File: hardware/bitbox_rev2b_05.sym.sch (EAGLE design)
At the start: 65 parts, among them IC3 LM317MSTT3, Q1 8MHz, U1 USD-SOCKETNEW, X2 2510-

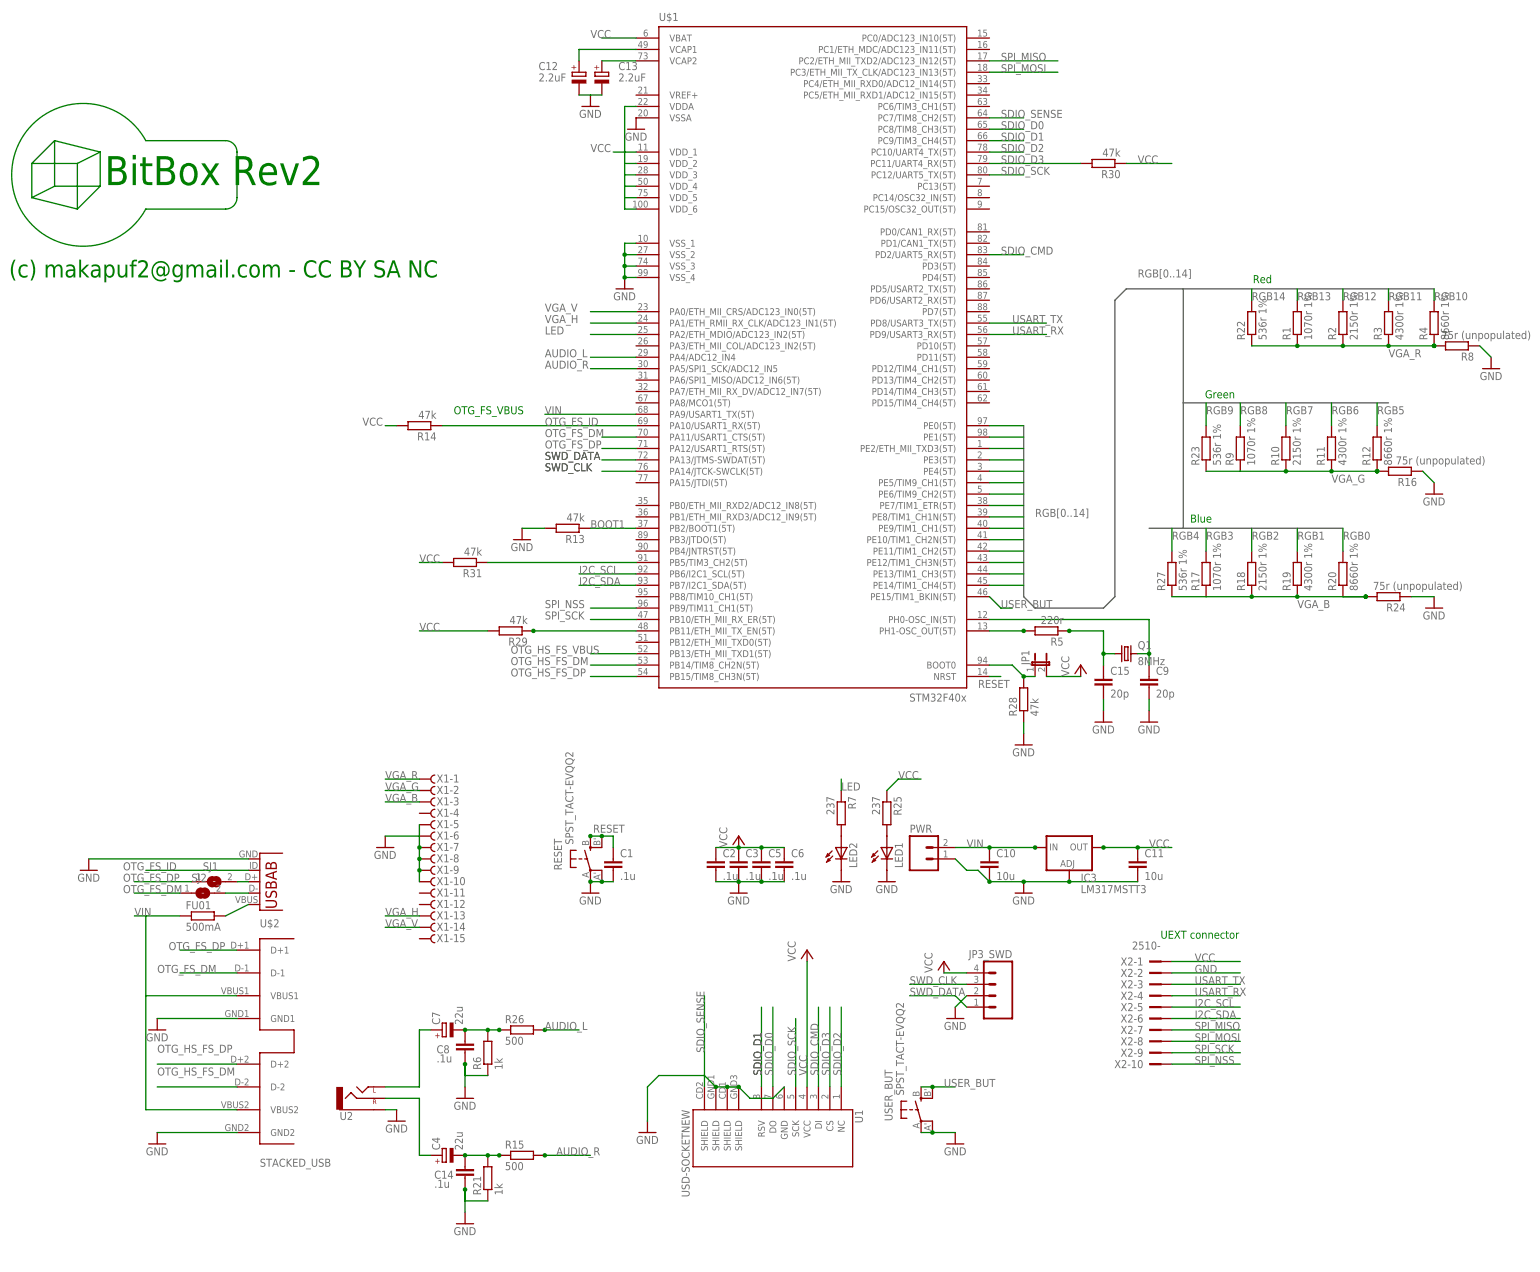
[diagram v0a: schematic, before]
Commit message: updated hardware eagle files to version 2.5 (also called 2b)
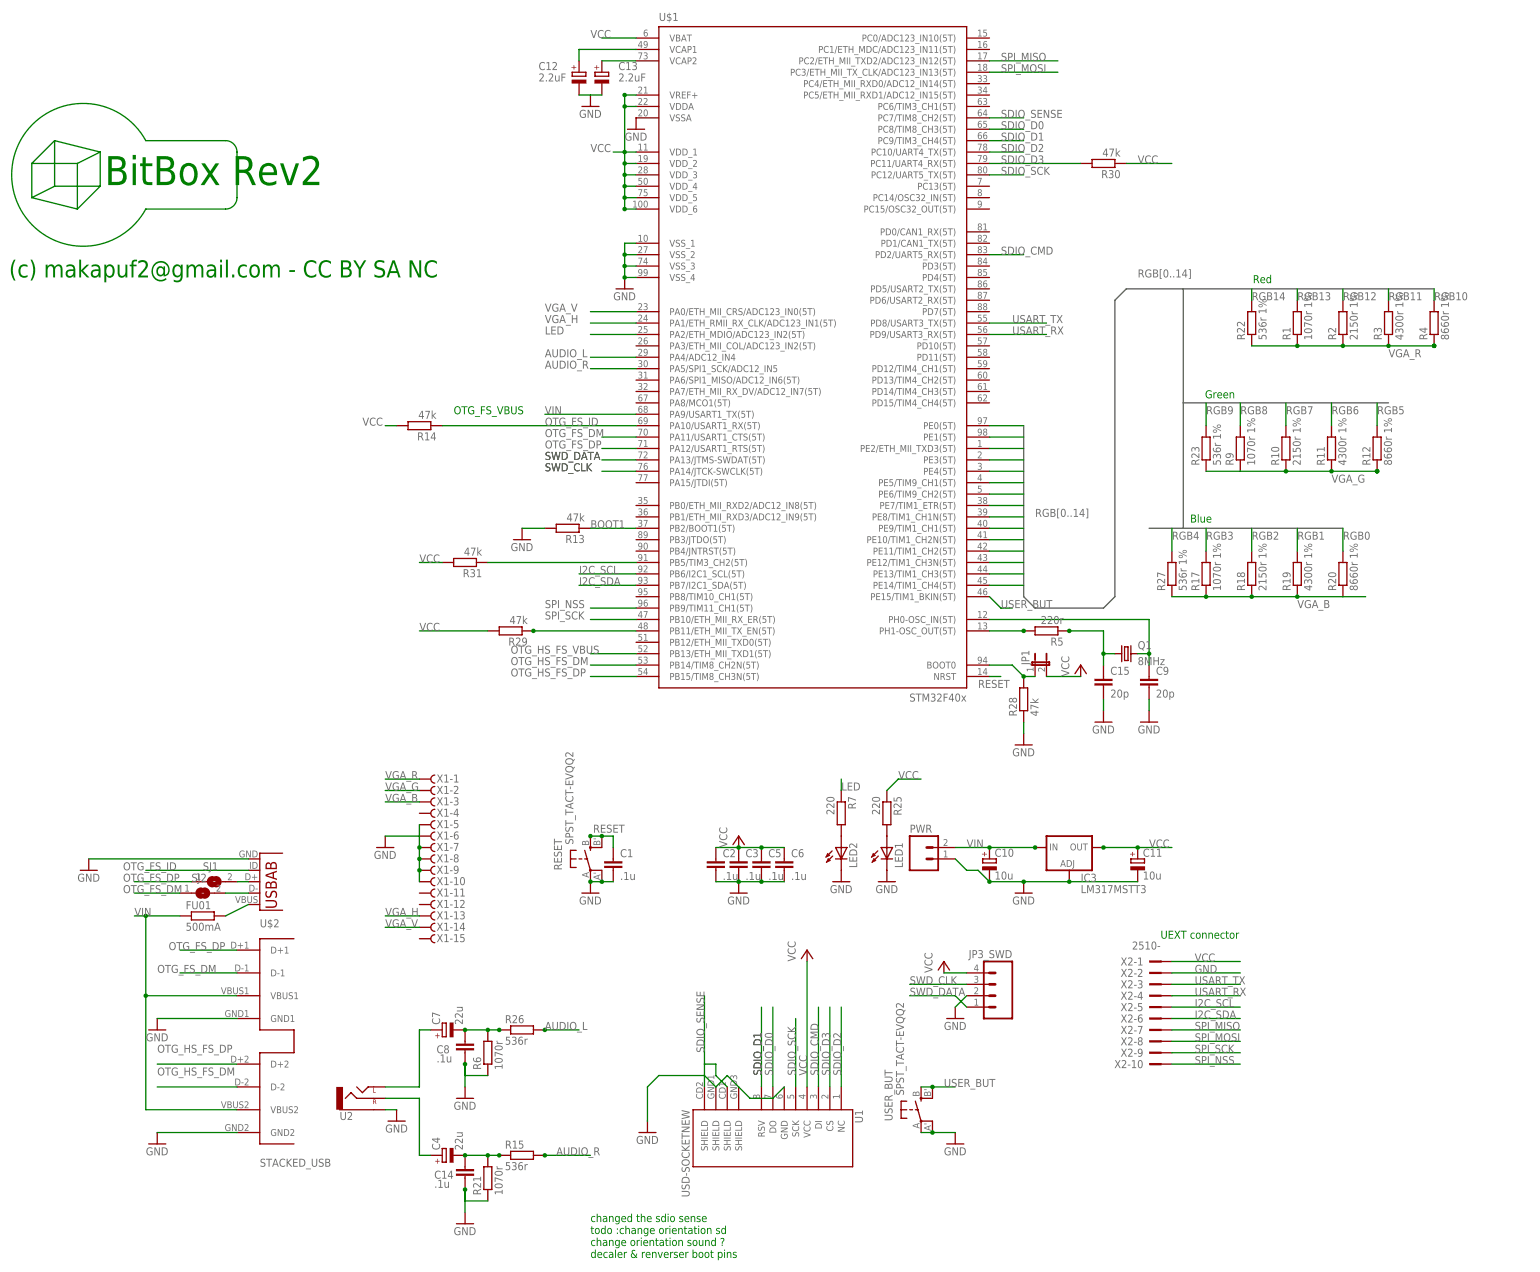
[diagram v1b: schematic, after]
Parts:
- removed R16, R24, R8: 75r (unpopulated), resistor:R-EU_R0603
- C10, C11: device resistor:C-EUC1206 -> resistor:CPOL-EUSMCA
- C12, C13: device resistor:CPOL-EUSMCB -> resistor:CPOL-EUSMCA
- R15, R26: value 500 -> 536r
- R21, R6: value 1k -> 1070r
- R25, R7: value 237 -> 220
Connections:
- net GND: now also C10.-, C11.-; no longer C10.2, C11.2, R16.1, R24.1, R8.1, U1.SHIELD@2
- net SDIO_SENSE: now also U1.SHIELD@2
- net VCC: now also C11.+, U$1.VREF+; no longer C11.1
- net VGA_B: no longer R24.2
- net VGA_G: no longer R16.2
- net VGA_R: no longer R8.2
- net VIN: now also C10.+; no longer C10.1
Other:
- note added: "changed the sdio sense todo :change orientation sd change orientation sound ? decaler & renverser boot pins"
